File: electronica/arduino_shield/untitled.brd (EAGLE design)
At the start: 68.6 x 54.3 mm, 16 parts

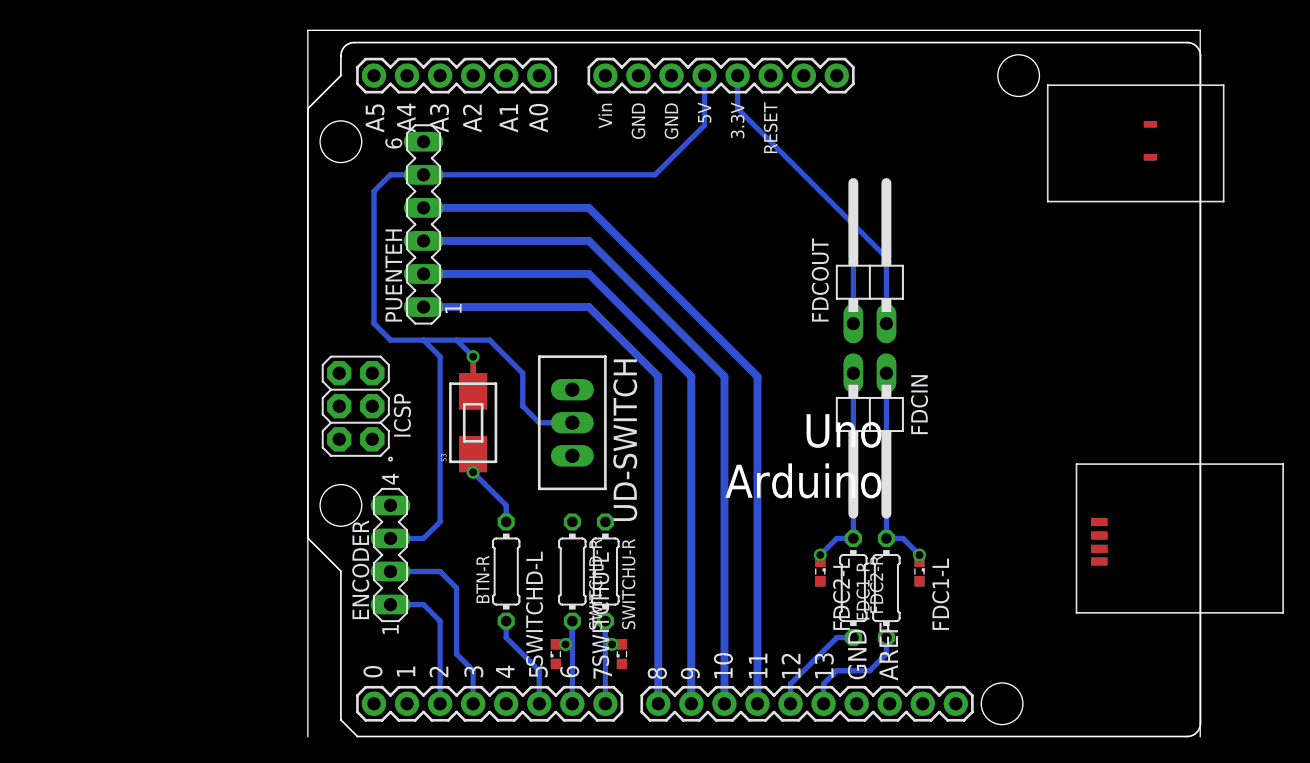
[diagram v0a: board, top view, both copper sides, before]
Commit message: shield arduino terminado
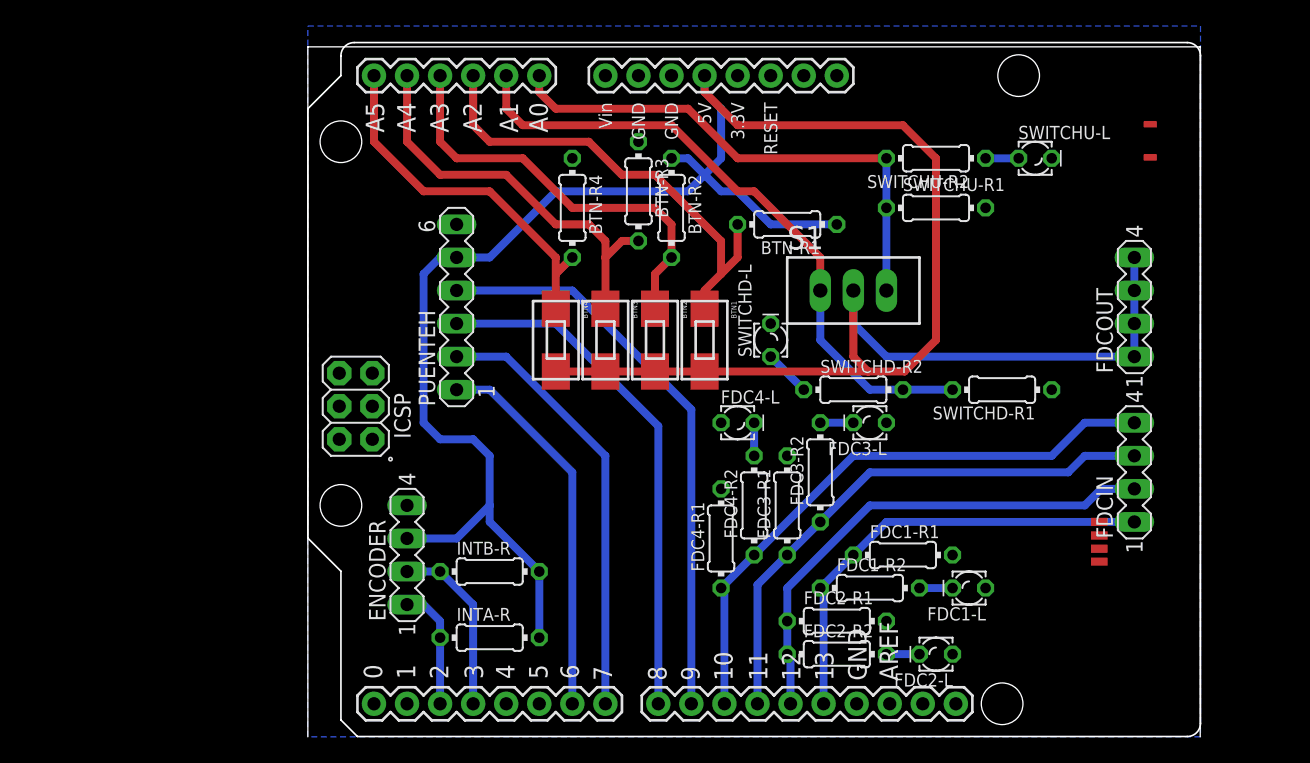
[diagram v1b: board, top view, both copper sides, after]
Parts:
- removed BTN-R, FDC1-R, FDC2-R, SWITCHD-R, SWITCHU-R: (no value), resistor:0204/7
- removed S3: (no value), eswitch-tact:TL3303_J
- removed UD-SWITCH: TL37PO, switch:TL3XPO
- added BTN-R1, BTN-R2, BTN-R3, BTN-R4, INTA-R, INTB-R, SWITCHD-R1, SWITCHU-R1: 1000, resistor:0204/7
- added BTN1, BTN2, BTN3, BTN4: 0, eswitch-tact:TL3303_J
- added FDC1-R1, FDC1-R2, FDC2-R1, FDC2-R2, FDC3-R1, FDC3-R2, FDC4-R1, FDC4-R2: (no value), resistor:0204/7
- added FDC3-L, FDC4-L: (no value), eagle-ltspice:LED_LD260
- added S1: TL39PO, switch:TL3XPO
- added SWITCHD-R2, SWITCHU-R2: 330, resistor:0204/7
- ENCODER: value (none) -> 1
- FDC1-L, FDC2-L, SWITCHD-L, SWITCHU-L: device eagle-ltspice:LED_SML0603 -> eagle-ltspice:LED_LD260
- FDCIN: value (none) -> 3; device pinhead:1X02/90 -> con-lstb:MA04-1
- FDCOUT: value (none) -> 2; device pinhead:1X02/90 -> con-lstb:MA04-1
- PUENTEH: value (none) -> 4
- moved SWITCHU-L 49.6 mm to (55.9, 44.5), turned to 0 degrees
- moved SWITCHD-L 29.2 mm to (35.6, 30.5)
- moved FDCIN 20.7 mm to (63.5, 20.3), turned to 90 degrees
- moved FDCOUT 20.5 mm to (63.5, 33.0), turned to 90 degrees
- moved FDC2-L 10.9 mm to (48.3, 6.35), turned to 180 degrees
- moved PUENTEH 6.84 mm to (11.4, 33.0)
- moved FDC1-L 4.02 mm to (50.8, 11.4), turned to 180 degrees
- moved ENCODER 1.27 mm to (7.62, 14.0)
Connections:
- removed net 3.3V: FDCOUT.1, FDCOUT.2, PCB1.3.3V
- removed net BTNIN: BTN-R.1, PCB1.5
- removed net N$5: BTN-R.2, S3.1
- new net BTN-IN1: BTN-R1.2, BTN1.1, PCB1.A2
- new net BTN-IN2: BTN-R2.2, BTN2.1, PCB1.A3
- new net BTN-IN3: BTN-R3.2, BTN3.1, PCB1.A4
- new net BTN-IN4: BTN-R4.2, BTN4.1, PCB1.A5
- new net FDC3: FDC3-R1.1, FDC3-R2.1, FDCIN.3, PCB1.11
- new net FDC4: FDC4-R1.1, FDC4-R2.1, FDCIN.4, PCB1.10
- new net N$6: FDC3-L.K, FDC3-R2.2
- new net N$7: FDC4-L.K, FDC4-R2.2
- net 5V: now also BTN1.2, BTN2.2, BTN3.2, BTN4.2, FDCOUT.1, FDCOUT.2, FDCOUT.3, FDCOUT.4, INTA-R.2, INTB-R.2, S1.2; no longer S3.2, UD-SWITCH.2
- net D1: now also PCB1.8; no longer PCB1.10
- net D2: now also PCB1.7; no longer PCB1.9
- net D3: now also PCB1.6; no longer PCB1.8
- net FDC1: now also FDC1-R1.1, FDC1-R2.1, FDCIN.1; no longer FDC1-R.1
- net FDC2: now also FDC2-R1.1, FDC2-R2.1, FDCIN.2; no longer FDC2-R.2
- net GND: now also BTN-R1.1, BTN-R2.1, BTN-R3.1, BTN-R4.1, FDC1-R1.2, FDC2-R1.2, FDC3-L.A, FDC3-R1.2, FDC4-L.A, FDC4-R1.2, PCB1.GND, SWITCHD-L.K, SWITCHD-R1.1, SWITCHU-L.K, SWITCHU-R1.2; no longer SWITCHD-L.C, SWITCHU-L.C
- net INTA: now also INTA-R.1
- net INTB: now also INTB-R.1
- net N$1: now also FDC1-L.K, FDC1-R2.2; no longer FDC1-L.C, FDC1-R.2, FDCIN.1
- net N$2: now also FDC2-L.K, FDC2-R2.2; no longer FDC2-L.C, FDC2-R.1, FDCIN.2
- net N$3: now also SWITCHU-L.A, SWITCHU-R2.1; no longer SWITCHU-R.1, UD-SWITCH.3
- net N$4: now also SWITCHD-L.A, SWITCHD-R2.1; no longer SWITCHD-R.1, UD-SWITCH.1
- net PWM: now also PCB1.9; no longer PCB1.11
- net SWITCHD: now also PCB1.A1, S1.1, SWITCHD-R1.2, SWITCHD-R2.2; no longer PCB1.6, SWITCHD-L.A, SWITCHD-R.2
- net SWITCHU: now also PCB1.A0, S1.3, SWITCHU-R1.1, SWITCHU-R2.2; no longer PCB1.7, SWITCHU-L.A, SWITCHU-R.2
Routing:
- net 5V: track 84.7 -> 178.8 mm, vias 1 -> 0
- net FDC4: track 0.00 -> 46.0 mm
- net FDC3: track 0.00 -> 42.2 mm
- net SWITCHD: track 9.11 -> 49.5 mm, vias 1 -> 0
- net BTN-IN1: track 0.00 -> 36.6 mm
- net BTN-IN2: track 0.00 -> 32.5 mm
- net BTN-IN3: track 0.00 -> 31.7 mm
- net 3.3V: track 31.4 -> 0.00 mm
- net SWITCHU: track 9.11 -> 40.2 mm, vias 1 -> 0
- net FDC2: track 7.82 -> 38.8 mm
- net BTN-IN4: track 0.00 -> 28.5 mm
- net FDC1: track 8.57 -> 35.2 mm
- net D3: track 45.4 -> 29.3 mm
- net D2: track 49.0 -> 33.6 mm
- net GND: track 0.00 -> 14.8 mm
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- added copper zone on layer 16, net GND
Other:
- board size 68.6 x 54.3 mm -> 68.6 x 53.3 mm

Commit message: correccion de planos, adicion de potenciometro
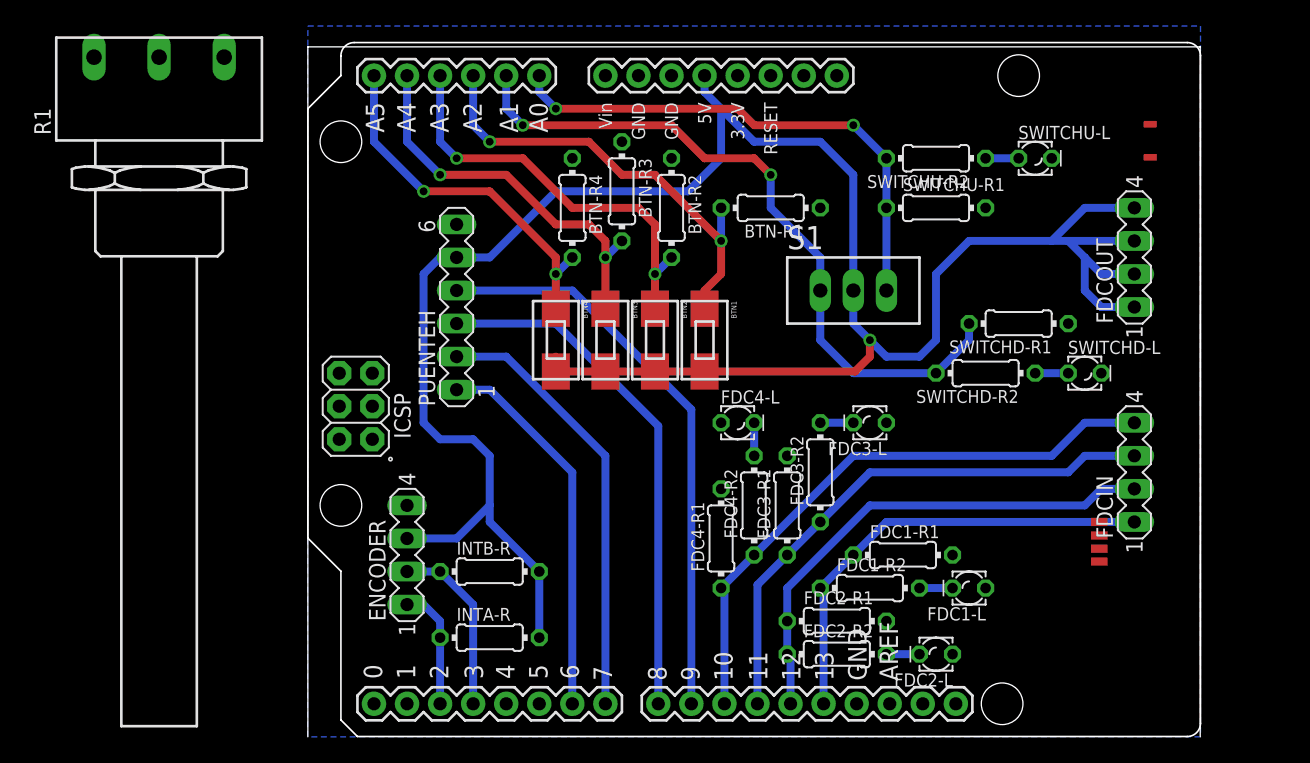
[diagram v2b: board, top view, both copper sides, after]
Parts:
- added R1: PC16S, piher:PC16S
- moved SWITCHD-L 24.3 mm to (59.7, 27.9), turned to 0 degrees
- moved SWITCHD-R2 10.2 mm to (52.1, 27.9), turned to 180 degrees
- moved SWITCHD-R1 5.24 mm to (54.6, 31.8)
- moved FDCOUT 3.81 mm to (63.5, 36.8)
- moved BTN-R1 1.80 mm to (35.6, 40.6)
- moved BTN-R3 1.27 mm to (24.1, 41.9)
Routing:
- net GND: track 14.8 -> 0.00 mm
- net SWITCHD: track 49.5 -> 54.0 mm, vias 0 -> 2
- net 5V: track 178.8 -> 174.4 mm, vias 0 -> 1
- net BTN-IN1: track 36.6 -> 34.8 mm, vias 0 -> 2
- net BTN-IN3: track 31.7 -> 30.5 mm, vias 0 -> 2
- net N$4: track 3.59 -> 2.54 mm
- net SWITCHU: vias 0 -> 2
- net BTN-IN2: vias 0 -> 2
- net BTN-IN4: vias 0 -> 2
